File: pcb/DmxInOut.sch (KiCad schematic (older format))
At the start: 59 parts, among them CON201 XLR3_F_GROUND, CON202 XLR3_M_GROUND, Q201 BC817, Q202 BC817, Q203 BC807, Q204 BC817, Q205 BC817, U201 SN75176, U202 6N137, U203 6N137, U204 AM2D-0505SZ, U205 SN75176, U206 PESD5V0S2BT, U207 PESD5V0S2BT

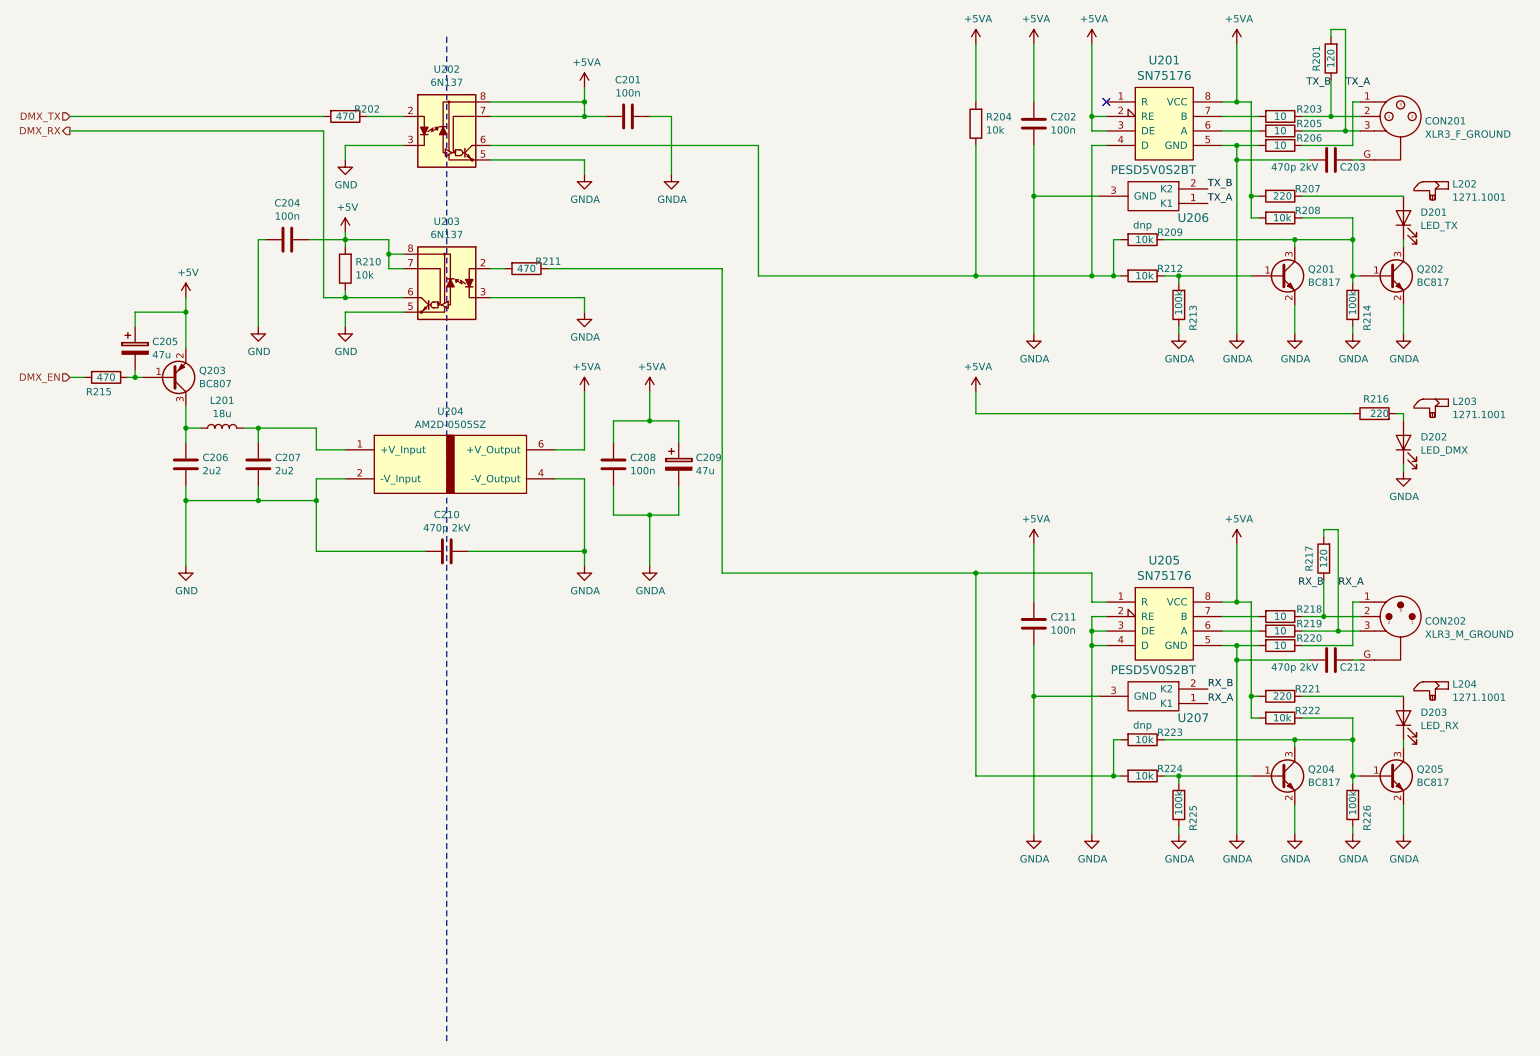
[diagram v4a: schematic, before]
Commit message: Bugfixing after testing prototype
Added a different pullup mechanism during programming to keep the USBN active during reset. Otherwise the ATmega loses its clock.
Fixed the broken pin association of the DMX connectors.
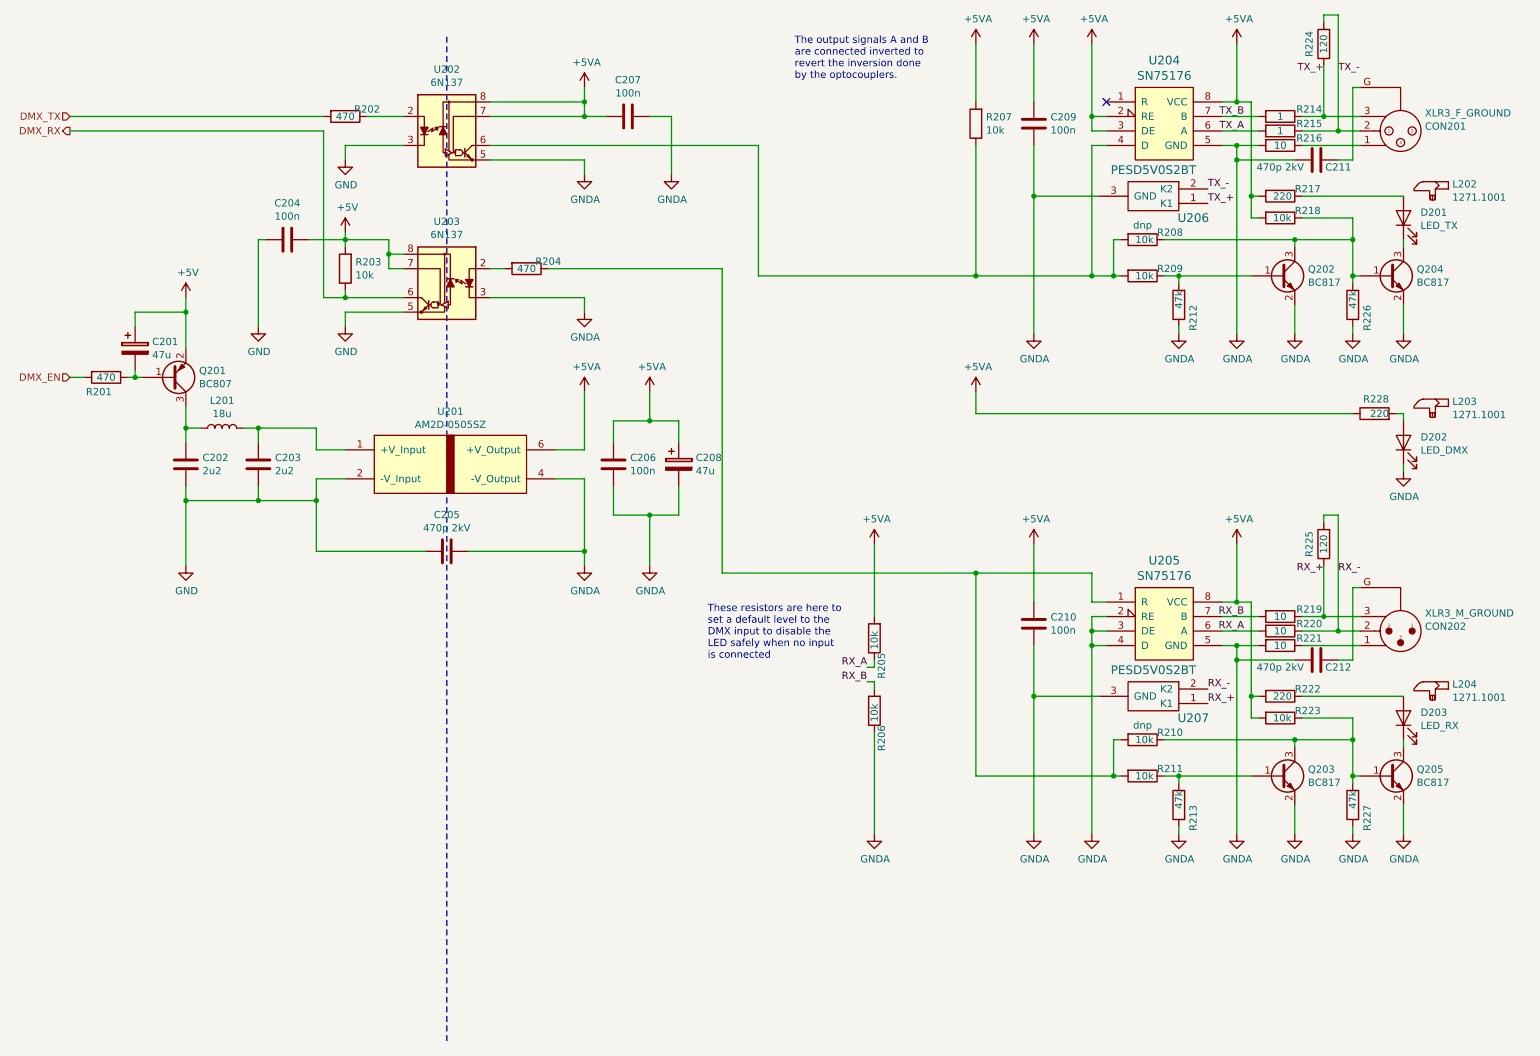
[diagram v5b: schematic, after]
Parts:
- added R205, R206: 10k, Resistors_SMD:R_0603_HandSoldering, symbol device:R
- R212: renamed from R213; value 100k -> 47k
- R213: renamed from R225; value 100k -> 47k
- R214: renamed from R203; value 10 -> 1
- R215: renamed from R205; value 10 -> 1
- R226: renamed from R214; value 100k -> 47k
- R227: renamed from R226; value 100k -> 47k
- renumbered C205 to C201, C206 to C202, C207 to C203, C210 to C205, C208 to C206, C201 to C207, C209 to C208, C202 to C209, C211 to C210, C203 to C211, Q203 to Q201, Q201 to Q202, Q204 to Q203, Q202 to Q204, R215 to R201, R210 to R203, R211 to R204, R204 to R207, R209 to R208, R212 to R209, R223 to R210, R224 to R211, R206 to R216, R207 to R217, R208 to R218, R218 to R219, R219 to R220, R220 to R221, R221 to R222, R222 to R223, R201 to R224, R217 to R225, R216 to R228, U204 to U201, U201 to U204
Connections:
- net +5VA: now also R205.2
- net GNDA: now also R206.1
- net RX_A: now also R220.2, U205.6 (A), R205.1; no longer CON202.3, R220.1, R225.2, U207.1 (K1)
- net RX_B: now also R219.2, U205.7 (B), R206.2; no longer CON202.2, R219.1, R225.1, U207.2 (K2)
- net TX_A: now also R215.2, U204.6 (A); no longer CON201.3, R215.1, R224.2, U206.1 (K1)
- net TX_B: now also R214.2, U204.7 (B); no longer CON201.2, R214.1, R224.1, U206.2 (K2)
- new net RX_+: CON202.3, R219.1, R225.1, U207.1 (K1)
- new net RX_-: CON202.2, R220.1, R225.2, U207.2 (K2)
- new net TX_+: CON201.3, R214.1, R224.1, U206.1 (K1)
- new net TX_-: CON201.2, R215.1, R224.2, U206.2 (K2)
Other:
- note added: "The output signals A and B\nare connected inverted to\nrevert the inversion done\nby the optocouplers."
- note added: "These resistors are here to\nset a default level to the\nDMX input to disable the\nLED safely when no input\nis connected"
- moved on the sheet: C211, C212, CON201, CON202, R224, R225

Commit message: fixed XLR connectors, LEDs and Reset
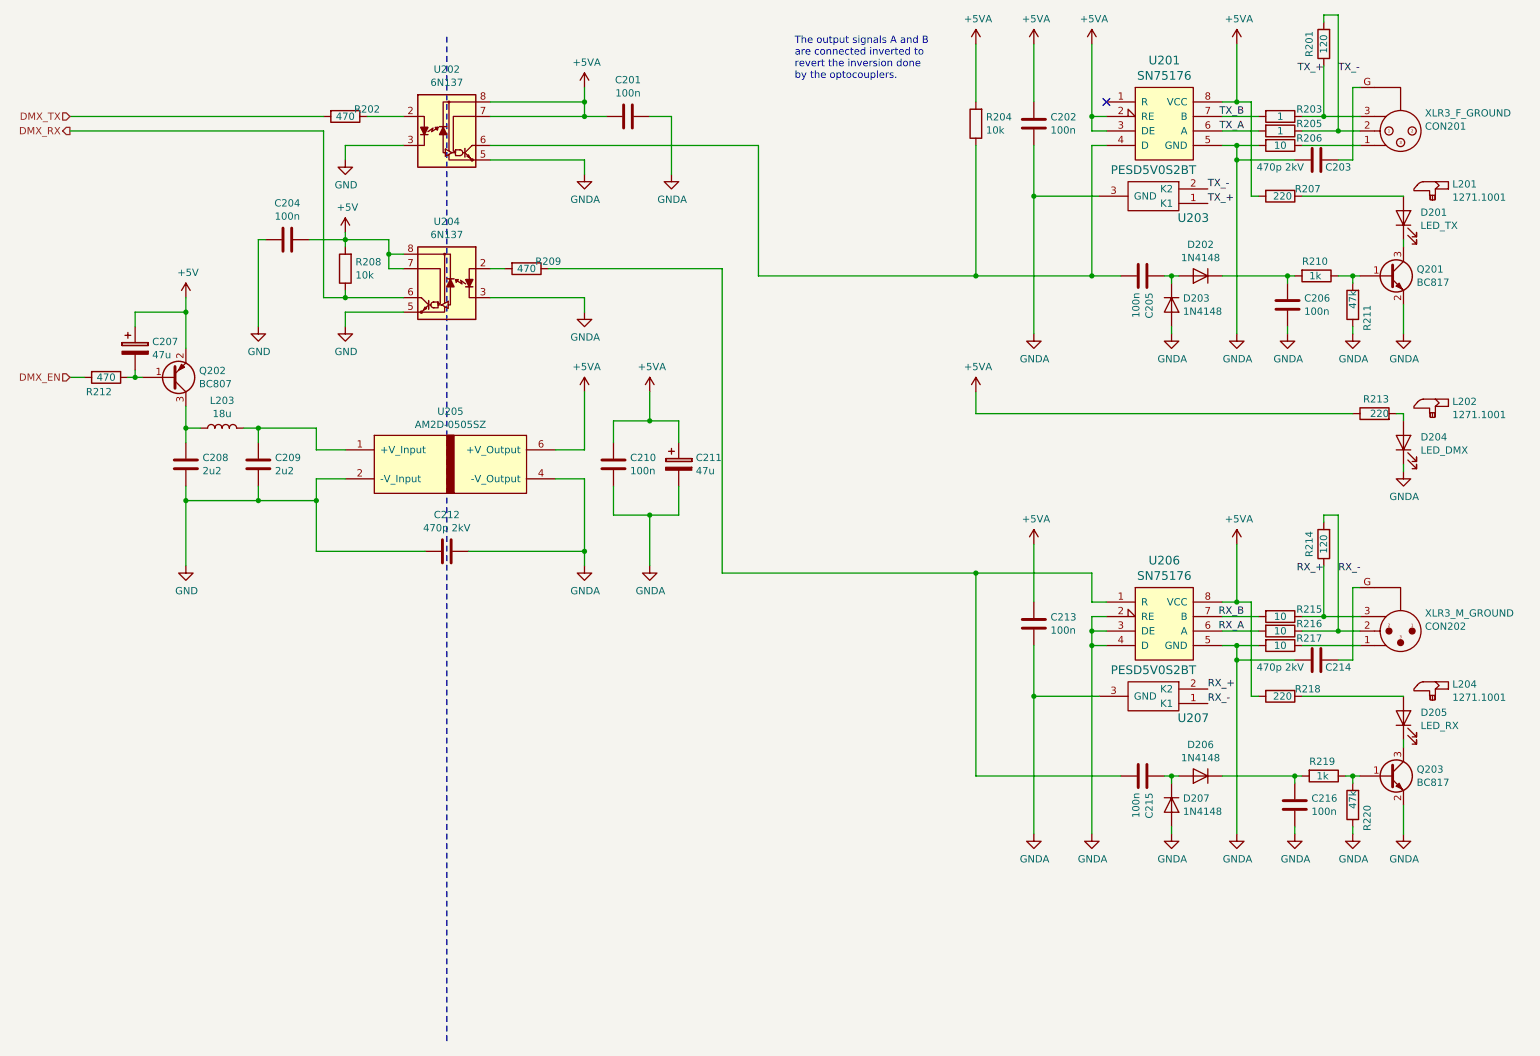
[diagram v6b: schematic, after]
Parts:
- removed Q202, Q203: BC817, TO_SOT_Packages_SMD:SOT-23, symbol Transistor_BJT:BC817
- removed R205, R206, R208, R210, R218, R223: 10k, Resistors_SMD:R_0603_HandSoldering, symbol device:R
- removed R212, R213: 47k, Resistors_SMD:R_0603_HandSoldering, symbol device:R
- added C205, C206, C215, C216: 100n, Capacitors_SMD:C_0603_HandSoldering, symbol device:C
- added D202, D203, D206, D207: 1N4148, Diodes_SMD:D_MiniMELF, symbol diode:1N4148
- R210: renamed from R209; value 10k -> 1k
- R219: renamed from R211; value 10k -> 1k
- renumbered C207 to C201, C209 to C202, C211 to C203, C201 to C207, C202 to C208, C203 to C209, C206 to C210, C208 to C211, C205 to C212, C210 to C213, C212 to C214, D202 to D204, D203 to D205, L202 to L201, L203 to L202, L201 to L203, Q204 to Q201, Q201 to Q202, Q205 to Q203, R224 to R201, R214 to R203, R207 to R204, R215 to R205, R216 to R206, R217 to R207, R203 to R208, R204 to R209, R226 to R211, R201 to R212, R228 to R213, R225 to R214, R219 to R215, R220 to R216, R221 to R217, R222 to R218, R227 to R220, U204 to U201, U206 to U203, U203 to U204, U201 to U205, U205 to U206
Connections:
- net GNDA: now also C206.1, C216.1, D203.2 (A), D207.2 (A)
- net RX_+: now also U207.2 (K2); no longer U207.1 (K1)
- net RX_-: now also U207.1 (K1); no longer U207.2 (K2)
- net at R204.1, U201.4 (D), U202.6: now also C205.1; no longer R210.2
- net at R209.1, U206.1 (R): now also C215.1; no longer R219.2
- net at Q201.1 (B), R211.2: now also R210.1
- net at Q203.1 (B), R220.2: now also R219.1
- new net: C206.2, D202.1 (K), R210.2
- new net: C216.2, D206.1 (K), R219.2
- new net: C205.2, D202.2 (A), D203.1 (K)
- new net: C215.2, D206.2 (A), D207.1 (K)
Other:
- note removed: "These resistors are here to\nset a default level to the\nDMX input to disable the\nLED safely when no input\nis connected"
- moved on the sheet: R210, R219

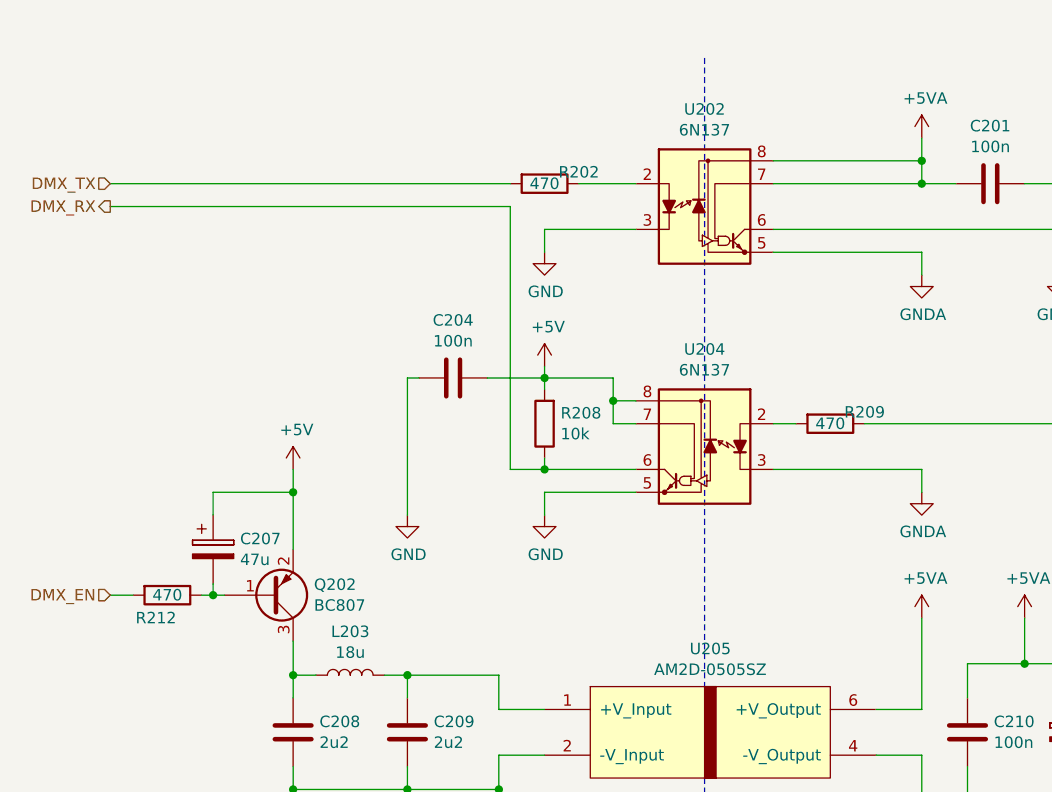
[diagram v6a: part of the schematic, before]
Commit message: changed footprints to fit better the real parts
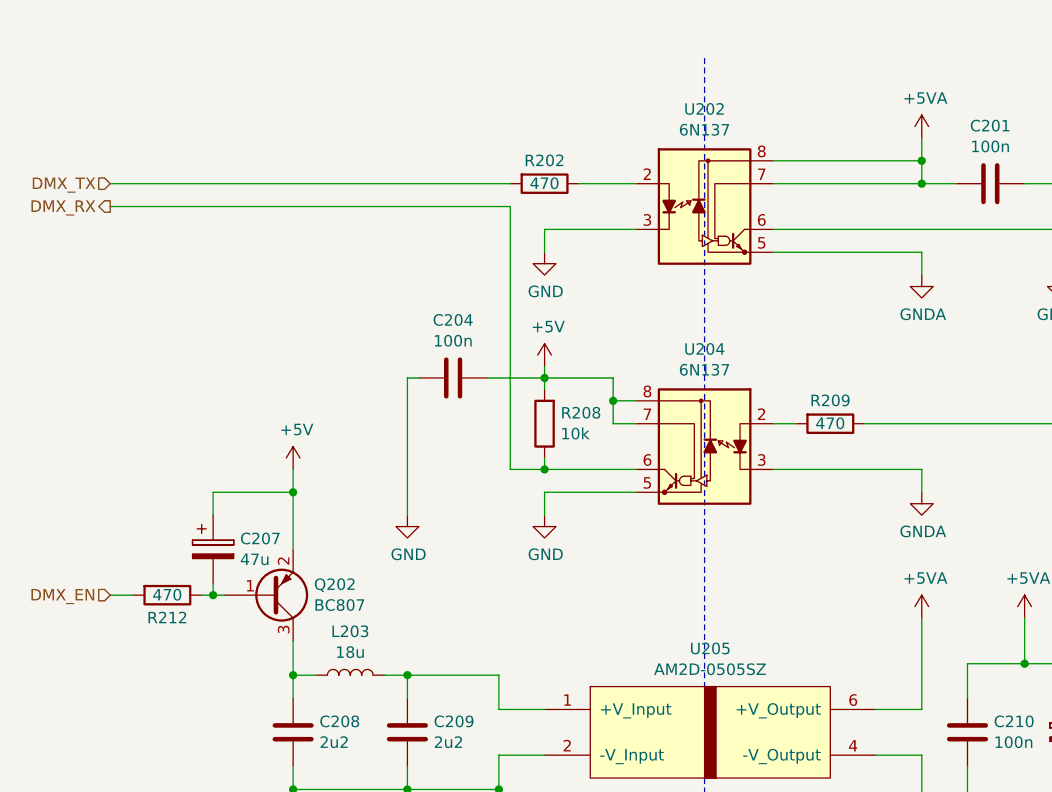
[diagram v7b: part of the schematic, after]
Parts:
- L203: footprint Resistors_SMD:R_1812_HandSoldering -> proz_choke:inductor_1812
- U201, U206: footprint Housings_SOIC:SO-8_5.3x6.2mm_Pitch1.27mm -> Power_Integrations:SO-8
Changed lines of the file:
@@
 F 0 "U201" H 8500 2237 60  0000 C CNN
 F 1 "SN75176" H 8500 2131 60  0000 C CNN
-F 2 "Housings_SOIC:SO-8_5.3x6.2mm_Pitch1.27mm" H 8250 1550 60  0001 C CNN
+F 2 "Power_Integrations:SO-8" H 8250 1550 60  0001 C CNN
 F 3 "" H 8250 1550 60  0000 C CNN
 	1    8250 1550
@@
 F 0 "L203" V 2190 3400 50  0000 C CNN
 F 1 "18u" V 2099 3400 50  0000 C CNN
-F 2 "Resistors_SMD:R_1812_HandSoldering" H 2000 3400 50  0001 C CNN
+F 2 "proz_choke:inductor_1812" H 2000 3400 50  0001 C CNN
 F 3 "~" H 2000 3400 50  0001 C CNN
 	1    2000 3400
@@
 U 1 1 5C042D2C
 P 1200 3050
-F 0 "R212" V 1300 3000 50  0000 C CNN
+F 0 "R212" V 1300 3050 50  0000 C CNN
 F 1 "470" V 1200 3050 50  0000 C CNN
 F 2 "Resistors_SMD:R_0603_HandSoldering" V 1130 3050 50  0001 C CNN
@@
 U 1 1 5C04DD71
 P 4100 2300
-F 0 "R209" V 4050 2450 50  0000 C CNN
+F 0 "R209" V 4000 2300 50  0000 C CNN
 F 1 "470" V 4100 2300 50  0000 C CNN
 F 2 "Resistors_SMD:R_0603_HandSoldering" V 4030 2300 50  0001 C CNN
@@
 F 0 "U206" H 8500 5687 60  0000 C CNN
 F 1 "SN75176" H 8500 5581 60  0000 C CNN
-F 2 "Housings_SOIC:SO-8_5.3x6.2mm_Pitch1.27mm" H 8250 5000 60  0001 C CNN
+F 2 "Power_Integrations:SO-8" H 8250 5000 60  0001 C CNN
 F 3 "" H 8250 5000 60  0000 C CNN
 	1    8250 5000
@@
 U 1 1 5C2655B1
 P 2850 1250
-F 0 "R202" V 2800 1400 50  0000 C CNN
+F 0 "R202" V 2750 1250 50  0000 C CNN
 F 1 "470" V 2850 1250 50  0000 C CNN
 F 2 "Resistors_SMD:R_0603_HandSoldering" V 2780 1250 50  0001 C CNN

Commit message: Updated all KiCad symbols and footprints to the ones on the current master branch of their symbols created all documents to produce this thing
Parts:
- C201, C202, C204, C205, C206, C210, C213, C215, C216: footprint Capacitors_SMD:C_0603_HandSoldering -> Capacitor_SMD:C_0603_1608Metric_Pad1.05x0.95mm_HandSolder; symbol device:C -> Device:C
- C203, C212, C214: footprint Capacitors_THT:C_Disc_D7.5mm_W5.0mm_P7.50mm -> Capacitor_THT:C_Disc_D7.5mm_W5.0mm_P7.50mm; symbol device:C -> Device:C
- C207, C211: footprint Capacitors_THT:CP_Radial_D5.0mm_P2.00mm -> Capacitor_THT:CP_Radial_D5.0mm_P2.00mm; symbol device:CP -> Device:CP
- C208, C209: footprint Capacitors_SMD:C_0805_HandSoldering -> Capacitor_SMD:C_0805_2012Metric_Pad1.15x1.40mm_HandSolder; symbol device:C -> Device:C
- D201, D204, D205: symbol device:LED -> Device:LED
- D202, D203, D206, D207: footprint Diodes_SMD:D_MiniMELF -> Diode_SMD:D_MiniMELF; symbol diode:1N4148 -> Diode:1N4148
- L203: symbol device:L -> Device:L
- Q201, Q202, Q203: footprint TO_SOT_Packages_SMD:SOT-23 -> Package_TO_SOT_SMD:SOT-23
- R201, R203, R205, R206, R214, R215, R216, R217: footprint Resistors_SMD:R_MiniMELF_MMA-0204 -> Resistor_SMD:R_MiniMELF_MMA-0204; symbol device:R -> Device:R
- R202, R204, R207, R208, R209, R210, R211, R212, R213, R218, R219, R220: footprint Resistors_SMD:R_0603_HandSoldering -> Resistor_SMD:R_0603_1608Metric_Pad1.05x0.95mm_HandSolder; symbol device:R -> Device:R
- U201, U206: footprint Power_Integrations:SO-8 -> Package_SO:SO-8_3.9x4.9mm_P1.27mm
- U203, U207: footprint TO_SOT_Packages_SMD:SOT-23_Handsoldering -> Package_TO_SOT_SMD:SOT-23_Handsoldering
